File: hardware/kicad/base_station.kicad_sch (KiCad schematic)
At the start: 4 parts, among them U1 Arduino UNO Q (STM32U585 side), U2 SmartElex KX134-1211 (acceler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, U3 INMP441 (I2S microphone), U4 WS2812B x8 status ring

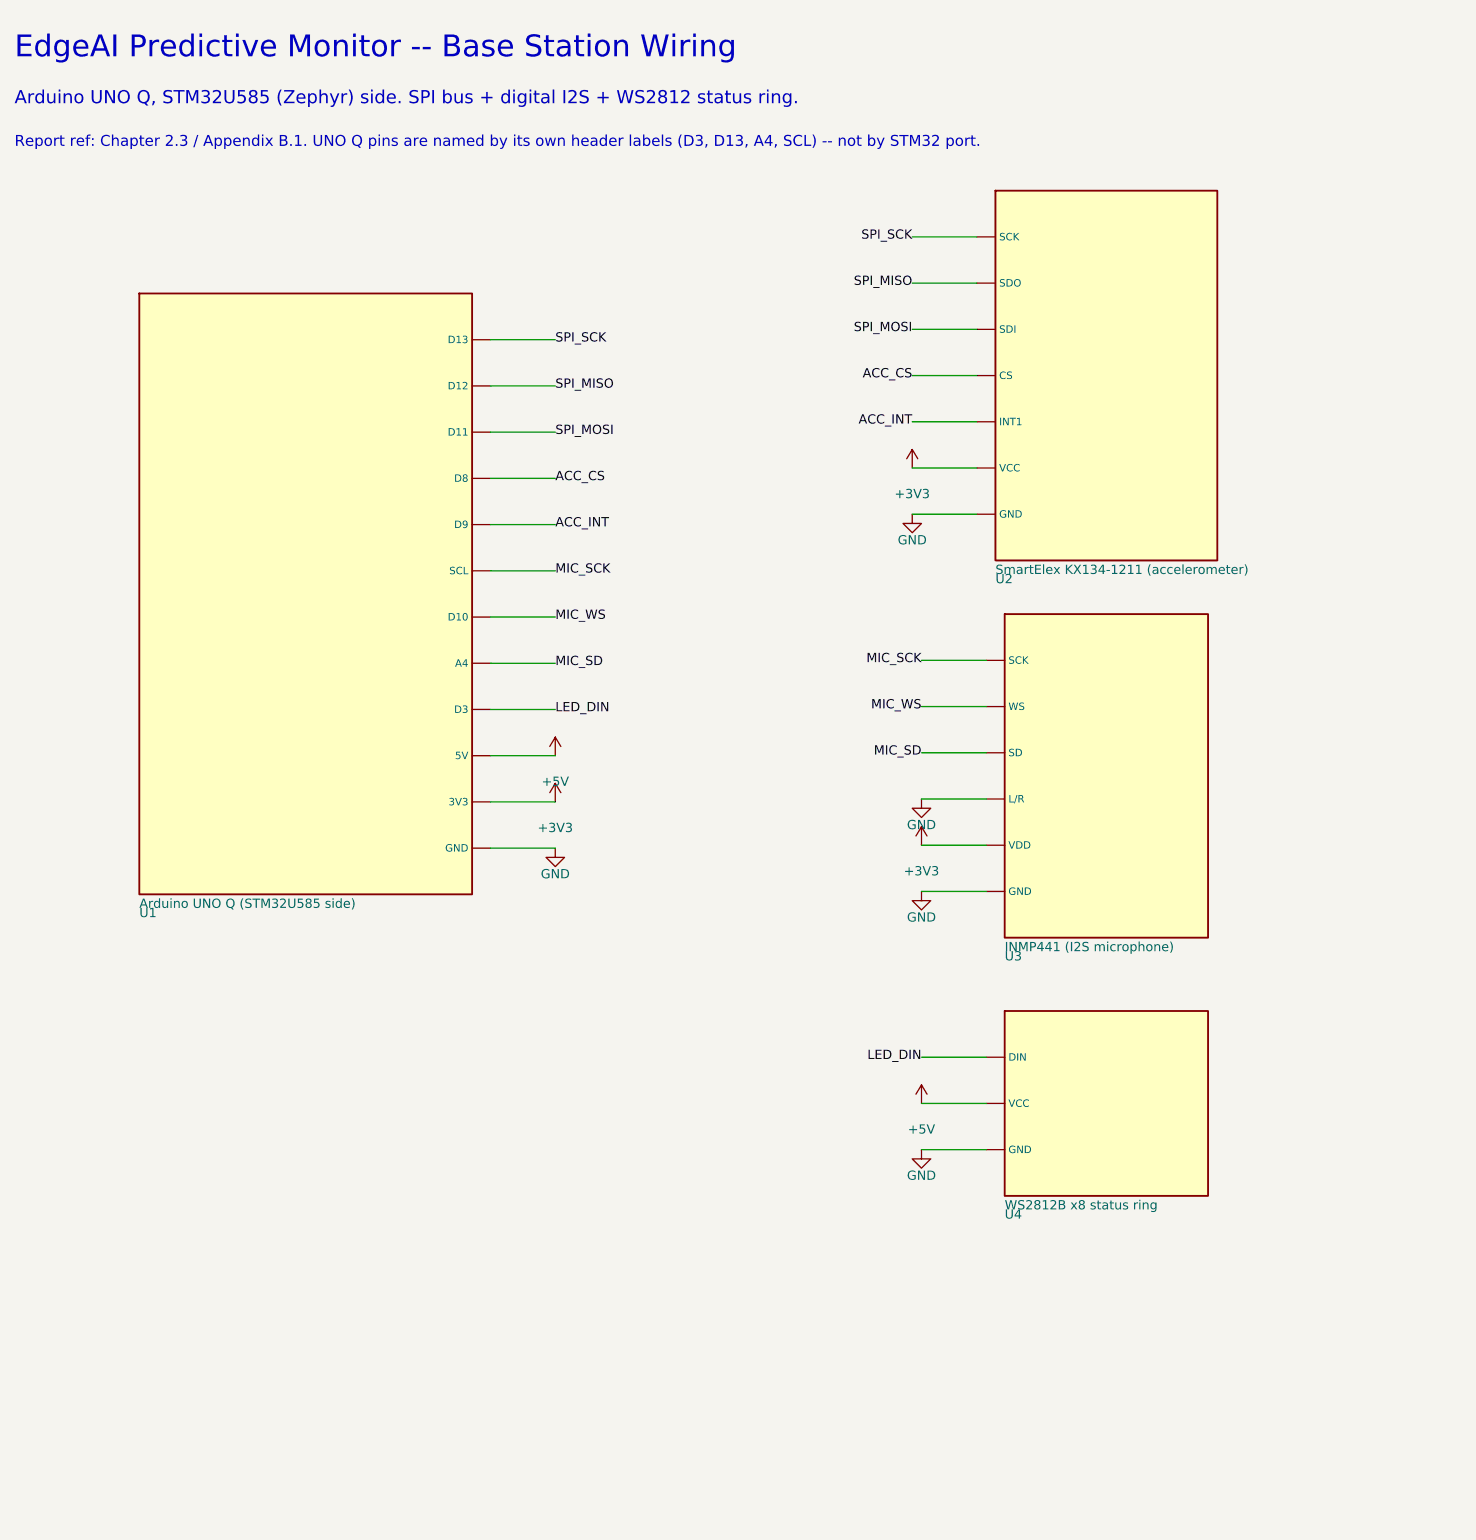
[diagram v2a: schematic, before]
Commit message: schematics: drop report-ref line, enlarge text, tighten crop
The report ref (Chapter/Appendix) was tied to a report structure the
submitted template doesn't use, so it's gone -- the useful pin-naming
and trimpot notes it was bundled with stayed. Separately, headings,
pin names, and net labels were too small to read once pasted into a
Word doc, so all text sizes went up in gen.py; row spacing now derives
from each part's real box height (via a new stack_column() helper)
instead of fixed y-coordinates, since the bigger fonts no longer fit
the old hand-picked positions. Crop step now masks out just the
title-block corner instead of scanning a fixed window, which cuts the
white margin around each exported PNG/PDF down to ~25px.

Co-Authored-By: Claude Sonnet 5 <noreply@anthropic.com>
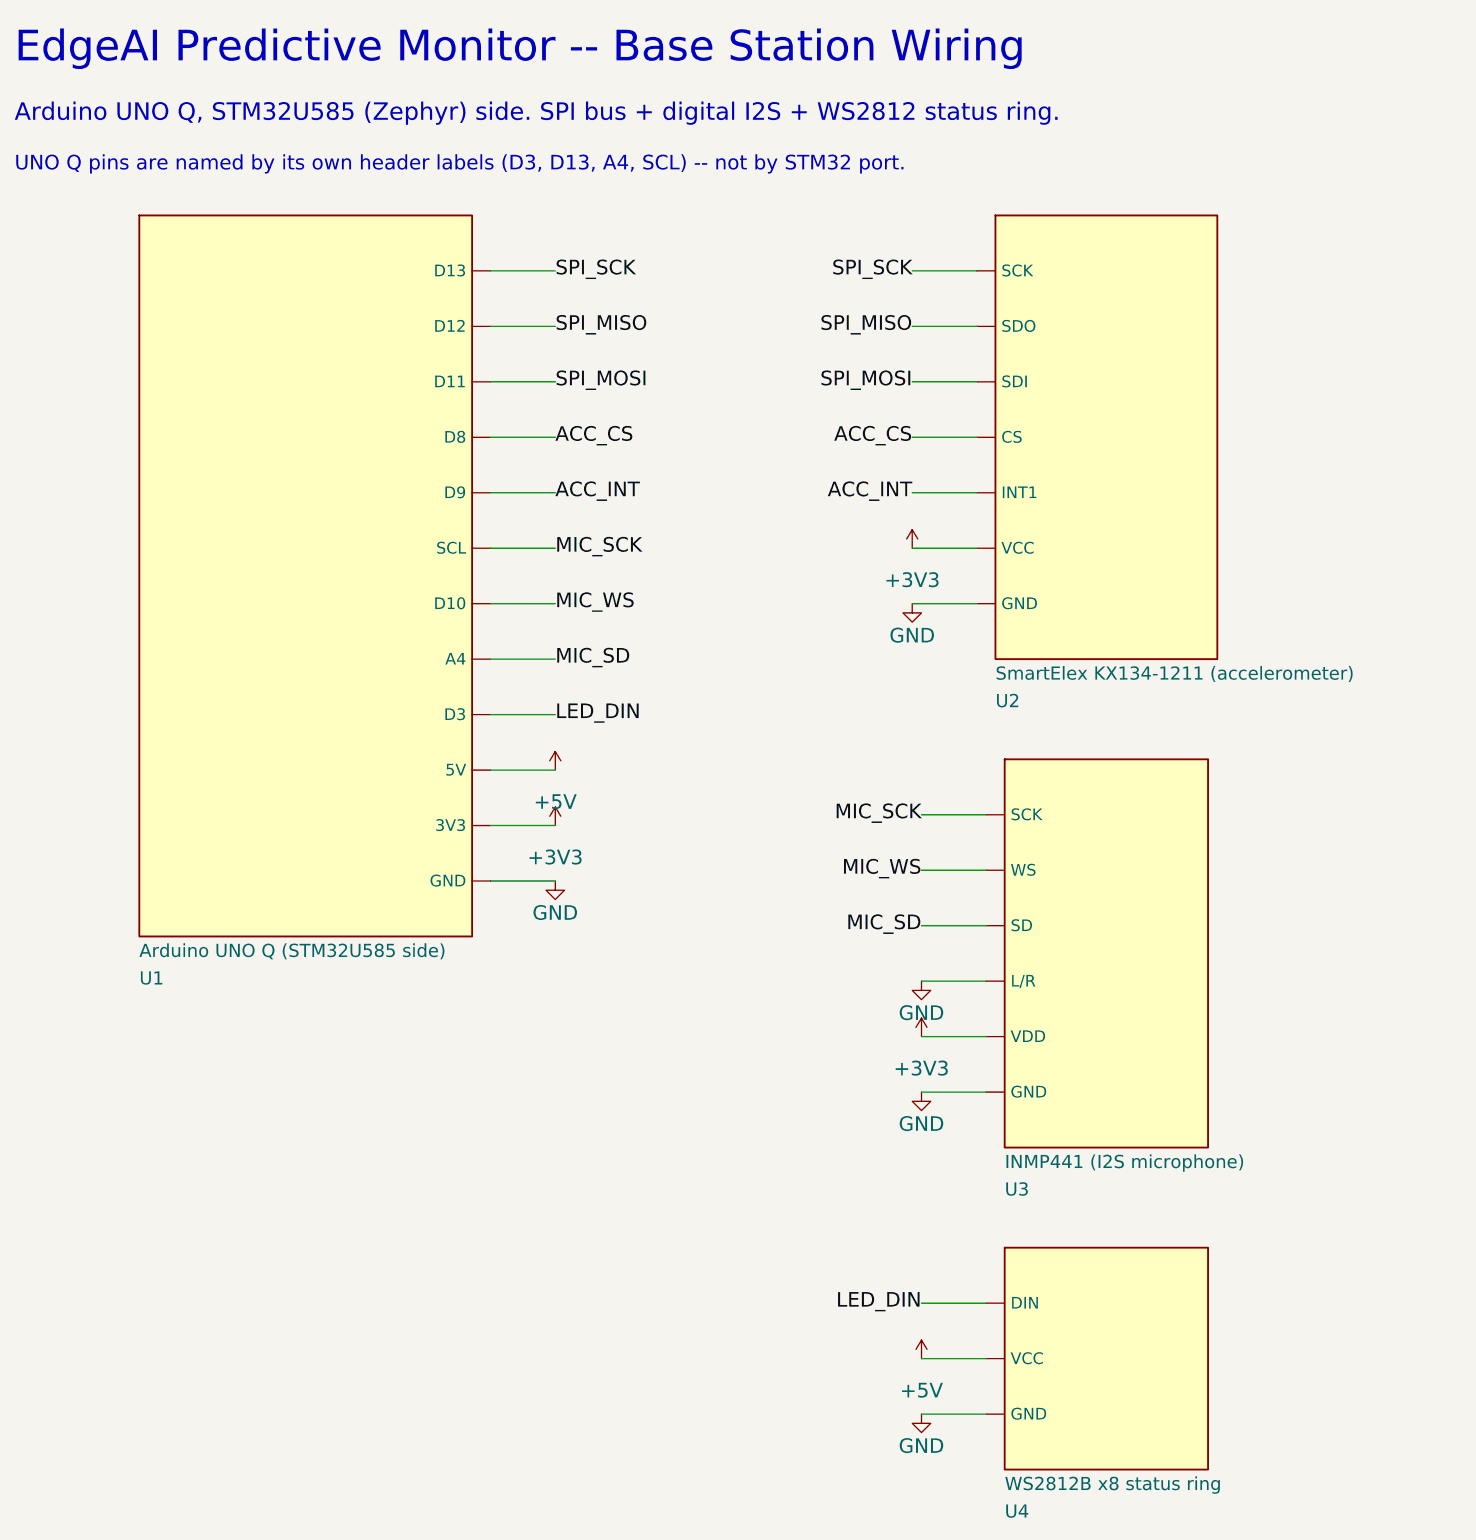
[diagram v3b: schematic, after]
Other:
- note added: "UNO Q pins are named by its own header labels (D3, D13, A4, SCL) -- not by STM32 port."
- note removed: "Report ref: Chapter 2.3 / Appendix B.1. UNO Q pins are named by its own header labels (D3, D13, A4, SCL) -- not by STM32 port."

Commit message: schematics: fix satellite pin map, rename accel nets, hi-res exports, KiCad projects
- satellite_node: ACC_CS/ACC_INT/MIC_WS/MIC_SD were wrong vs
  satellite/include/board_pins.h (used D3/D2/D0/D4; firmware drives
  D6/D7/D2/D3). Now transcribed straight from the header.
- base + satellite: SPI_SCK/MISO/MOSI nets renamed to ACC_SCK/ACC_MISO/
  ACC_MOSI so the accelerometer bus reads consistently with ACC_CS/ACC_INT.
- exports: SVG now --exclude-drawing-sheet; raster bumped to scale=5.0
  (~3.6-3.9k px) for headroom against Hackster's imgix auto=compress;
  report PNGs flattened to true PNG-24 (no alpha) + sibling JPEGs (q92).
  Crop simplified to a plain ink bbox.
- gen.py write_pro() now emits a real minimal .kicad_pro per board
  (sheets -> sch root UUID) so each opens as a self-contained project;
  make_bundles.py zips pro+sch+pdf into dist/ for Hackster Attachments
  (dist/ git-ignored).

Co-Authored-By: Claude Sonnet 5 <noreply@anthropic.com>
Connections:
- net SPI_MISO renamed ACC_MISO
- net SPI_MOSI renamed ACC_MOSI
- net SPI_SCK renamed ACC_SCK
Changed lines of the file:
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@@
 		(stroke (width 0) (type default))
 	)
-	(label "SPI_SCK"
+	(label "ACC_SCK"
 		(at 94.29 55.62 0)
 		(effects (font (size 2.0 2.0)) (justify left))
 	)
-	(label "SPI_MISO"
+	(label "ACC_MISO"
 		(at 94.29 63.24 0)
 		(effects (font (size 2.0 2.0)) (justify left))
 	)
-	(label "SPI_MOSI"
+	(label "ACC_MOSI"
 		(at 94.29 70.86 0)
 		(effects (font (size 2.0 2.0)) (justify left))
@@
 		(effects (font (size 2.0 2.0)) (justify left))
 	)
-	(label "SPI_SCK"
+	(label "ACC_SCK"
 		(at 143.32999999999998 55.620000000000005 0)
 		(effects (font (size 2.0 2.0)) (justify right))
 	)
-	(label "SPI_MISO"
+	(label "ACC_MISO"
 		(at 143.32999999999998 63.24 0)
 		(effects (font (size 2.0 2.0)) (justify right))
 	)
-	(label "SPI_MOSI"
+	(label "ACC_MOSI"
 		(at 143.32999999999998 70.86 0)
 		(effects (font (size 2.0 2.0)) (justify right))
@@
 		(instances
 			(project "epm"
-				(path "/a0b76a3e-9992-4eb4-941e-e2004c422378"
+				(path "/a6210c52-d586-4da6-b3ef-d8550748d613"
 					(reference "U1")
 					(unit 1)
@@
 		(on_board yes)
 		(dnp no)
-		(property "Reference" "#PWR9a34"
+		(property "Reference" "#PWR5174"
 			(at 94.29 118.2 0)
 			(effects (font (size 1.27 1.27)) (hide yes))
@@
 		(instances
 			(project "epm"
-				(path "/a0b76a3e-9992-4eb4-941e-e2004c422378"
-					(reference "#PWR9a34")
+				(path "/a6210c52-d586-4da6-b3ef-d8550748d613"
+					(reference "#PWR5174")
 					(unit 1)
 				)
@@
 		(on_board yes)
 		(dnp no)
-		(property "Reference" "#PWR9c4a"
+		(property "Reference" "#PWR42f3"
 			(at 94.29 125.82 0)
 			(effects (font (size 1.27 1.27)) (hide yes))
@@
 		(instances
 			(project "epm"
-				(path "/a0b76a3e-9992-4eb4-941e-e2004c422378"
-					(reference "#PWR9c4a")
+				(path "/a6210c52-d586-4da6-b3ef-d8550748d613"
+					(reference "#PWR42f3")
 					(unit 1)
 				)
@@
 		(on_board yes)
 		(dnp no)
-		(property "Reference" "#PWRcb86"
+		(property "Reference" "#PWRe811"
 			(at 94.29 133.44 0)
 			(effects (font (size 1.27 1.27)) (hide yes))
@@
 		(instances
 			(project "epm"
-				(path "/a0b76a3e-9992-4eb4-941e-e2004c422378"
-					(reference "#PWRcb86")
+				(path "/a6210c52-d586-4da6-b3ef-d8550748d613"
+					(reference "#PWRe811")
 					(unit 1)
 				)
@@
 		(instances
 			(project "epm"
-				(path "/a0b76a3e-9992-4eb4-941e-e2004c422378"
+				(path "/a6210c52-d586-4da6-b3ef-d8550748d613"
 					(reference "U2")
 					(unit 1)
@@
 		(on_board yes)
 		(dnp no)
-		(property "Reference" "#PWR1375"
+		(property "Reference" "#PWRebb2"
 			(at 143.32999999999998 87.72 0)
 			(effects (font (size 1.27 1.27)) (hide yes))
@@
 		(instances
 			(project "epm"
-				(path "/a0b76a3e-9992-4eb4-941e-e2004c422378"
-					(reference "#PWR1375")
+				(path "/a6210c52-d586-4da6-b3ef-d8550748d613"
+					(reference "#PWRebb2")
 					(unit 1)
 				)
@@
 		(on_board yes)
 		(dnp no)
-		(property "Reference" "#PWRd943"
+		(property "Reference" "#PWR6b43"
 			(at 143.32999999999998 95.34 0)
 			(effects (font (size 1.27 1.27)) (hide yes))
@@
 		(instances
 			(project "epm"
-				(path "/a0b76a3e-9992-4eb4-941e-e2004c422378"
-					(reference "#PWRd943")
+				(path "/a6210c52-d586-4da6-b3ef-d8550748d613"
+					(reference "#PWR6b43")
 					(unit 1)
 				)
@@
 		(instances
 			(project "epm"
-				(path "/a0b76a3e-9992-4eb4-941e-e2004c422378"
+				(path "/a6210c52-d586-4da6-b3ef-d8550748d613"
 					(reference "U3")
 					(unit 1)
@@
 		(on_board yes)
 		(dnp no)
-		(property "Reference" "#PWRd4eb"
+		(property "Reference" "#PWRb736"
 			(at 144.60000000000002 147.20000000000002 0)
 			(effects (font (size 1.27 1.27)) (hide yes))
@@
 		(instances
 			(project "epm"
-				(path "/a0b76a3e-9992-4eb4-941e-e2004c422378"
-					(reference "#PWRd4eb")
+				(path "/a6210c52-d586-4da6-b3ef-d8550748d613"
+					(reference "#PWRb736")
 					(unit 1)
 				)
@@
 		(on_board yes)
 		(dnp no)
-		(property "Reference" "#PWRcfdb"
+		(property "Reference" "#PWR3c86"
 			(at 144.60000000000002 154.82000000000002 0)
 			(effects (font (size 1.27 1.27)) (hide yes))
@@
 		(instances
 			(project "epm"
-				(path "/a0b76a3e-9992-4eb4-941e-e2004c422378"
-					(reference "#PWRcfdb")
+				(path "/a6210c52-d586-4da6-b3ef-d8550748d613"
+					(reference "#PWR3c86")
 					(unit 1)
 				)
@@
 		(on_board yes)
 		(dnp no)
-		(property "Reference" "#PWR4bdb"
+		(property "Reference" "#PWR9344"
 			(at 144.60000000000002 162.44000000000003 0)
 			(effects (font (size 1.27 1.27)) (hide yes))
@@
 		(instances
 			(project "epm"
-				(path "/a0b76a3e-9992-4eb4-941e-e2004c422378"
-					(reference "#PWR4bdb")
+				(path "/a6210c52-d586-4da6-b3ef-d8550748d613"
+					(reference "#PWR9344")
 					(unit 1)
 				)
@@
 		(instances
 			(project "epm"
-				(path "/a0b76a3e-9992-4eb4-941e-e2004c422378"
+				(path "/a6210c52-d586-4da6-b3ef-d8550748d613"
 					(reference "U4")
 					(unit 1)
@@
 		(on_board yes)
 		(dnp no)
-		(property "Reference" "#PWRe348"
+		(property "Reference" "#PWR2466"
 			(at 144.60000000000002 199.06 0)
 			(effects (font (size 1.27 1.27)) (hide yes))
@@
 		(instances
 			(project "epm"
-				(path "/a0b76a3e-9992-4eb4-941e-e2004c422378"
-					(reference "#PWRe348")
+				(path "/a6210c52-d586-4da6-b3ef-d8550748d613"
+					(reference "#PWR2466")
 					(unit 1)
 				)
@@
 		(on_board yes)
 		(dnp no)
-		(property "Reference" "#PWR97b8"
+		(property "Reference" "#PWRd0ac"
 			(at 144.60000000000002 206.68 0)
 			(effects (font (size 1.27 1.27)) (hide yes))
@@
 		(instances
 			(project "epm"
-				(path "/a0b76a3e-9992-4eb4-941e-e2004c422378"
-					(reference "#PWR97b8")
-					(unit 1)
-				)
+				(path "/a6210c52-d586-4da6-b3ef-d8550748d613"
+					(reference "#PWRd0ac")
+					(unit 1)
+				)
